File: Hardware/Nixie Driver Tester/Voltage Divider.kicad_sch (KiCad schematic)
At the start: 2 parts

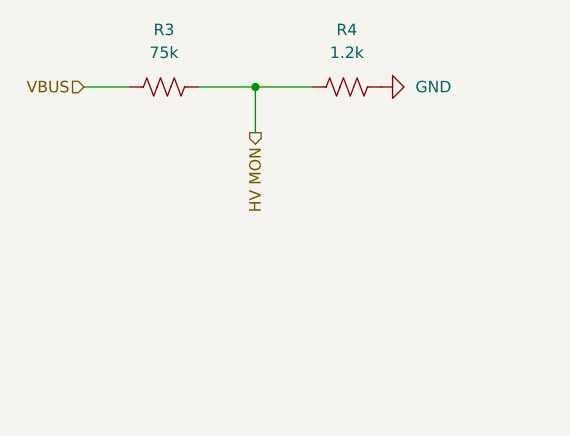
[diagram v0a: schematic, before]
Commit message: Added Nixie headers
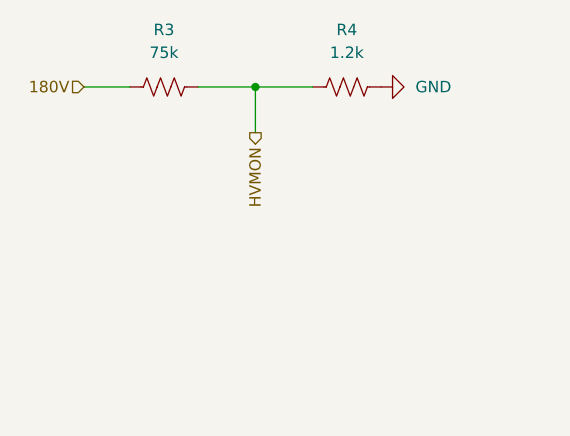
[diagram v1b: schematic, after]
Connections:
- net HV MON renamed HVMON
- net VBUS renamed 180V
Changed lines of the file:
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@@
 		)
 	)
-	(hierarchical_label "HV MON"
+	(hierarchical_label "HVMON"
 		(shape output)
 		(at 133.35 106.68 270)
@@
 		)
 	)
-	(hierarchical_label "VBUS"
+	(hierarchical_label "180V"
 		(shape input)
 		(at 114.3 101.6 180)

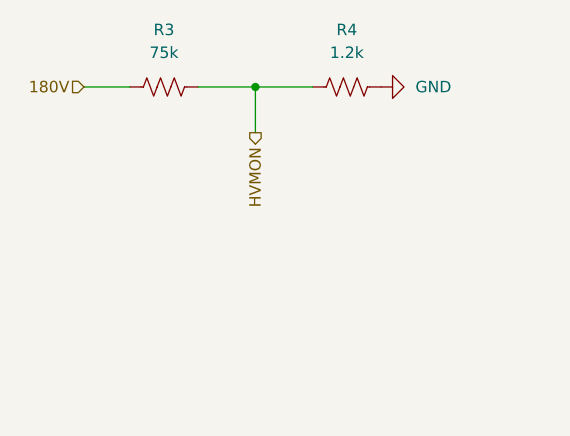
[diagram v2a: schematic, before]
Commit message: Shrunk the board vertically
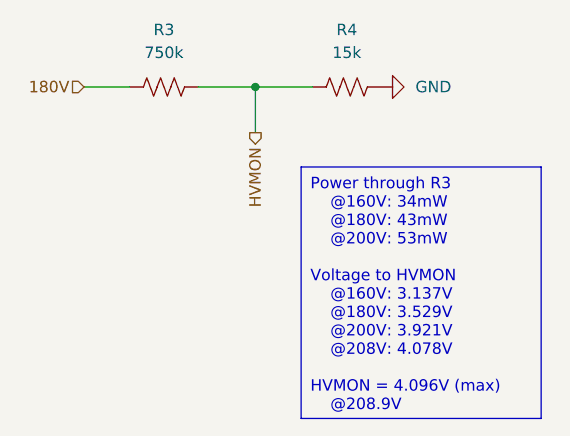
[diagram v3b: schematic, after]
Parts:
- R3: value 75k -> 750k
- R4: value 1.2k -> 15k
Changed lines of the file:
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@@
+		)
+	)
+	(text_box "Power through R3\n	@160V: 34mW\n	@180V: 43mW\n	@200V: 53mW\n\nVoltage to HVMON\n	@160V: 3.137V\n	@180V: 3.529V\n	@200V: 3.921V\n	@208V: 4.078V\n\nHVMON = 4.096V (max)\n	@208.9V"
+		(exclude_from_sim no)
+		(at 138.43 110.49 0)
+		(size 26.67 27.94)
+		(stroke
+			(width 0)
+			(type default)
+		)
+		(fill
+			(type none)
+		)
+		(effects
+			(font
+				(size 1.27 1.27)
+			)
+			(justify left top)
 		)
 	)
@@
 			)
 		)
-		(property "Value" "75k"
+		(property "Value" "750k"
 			(at 123.19 97.79 90)
 			(effects
@@
 			)
 		)
-		(property "Value" "1.2k"
+		(property "Value" "15k"
 			(at 143.51 97.79 90)
 			(effects
